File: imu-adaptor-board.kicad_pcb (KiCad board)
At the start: 2 copper layers, 49.5 x 49.5 mm, 7 parts, among them M3_MOUNT VAL**, P1 IMU-CAN, P2 IMU-SPI3, U1 ADIS16405BMLZ

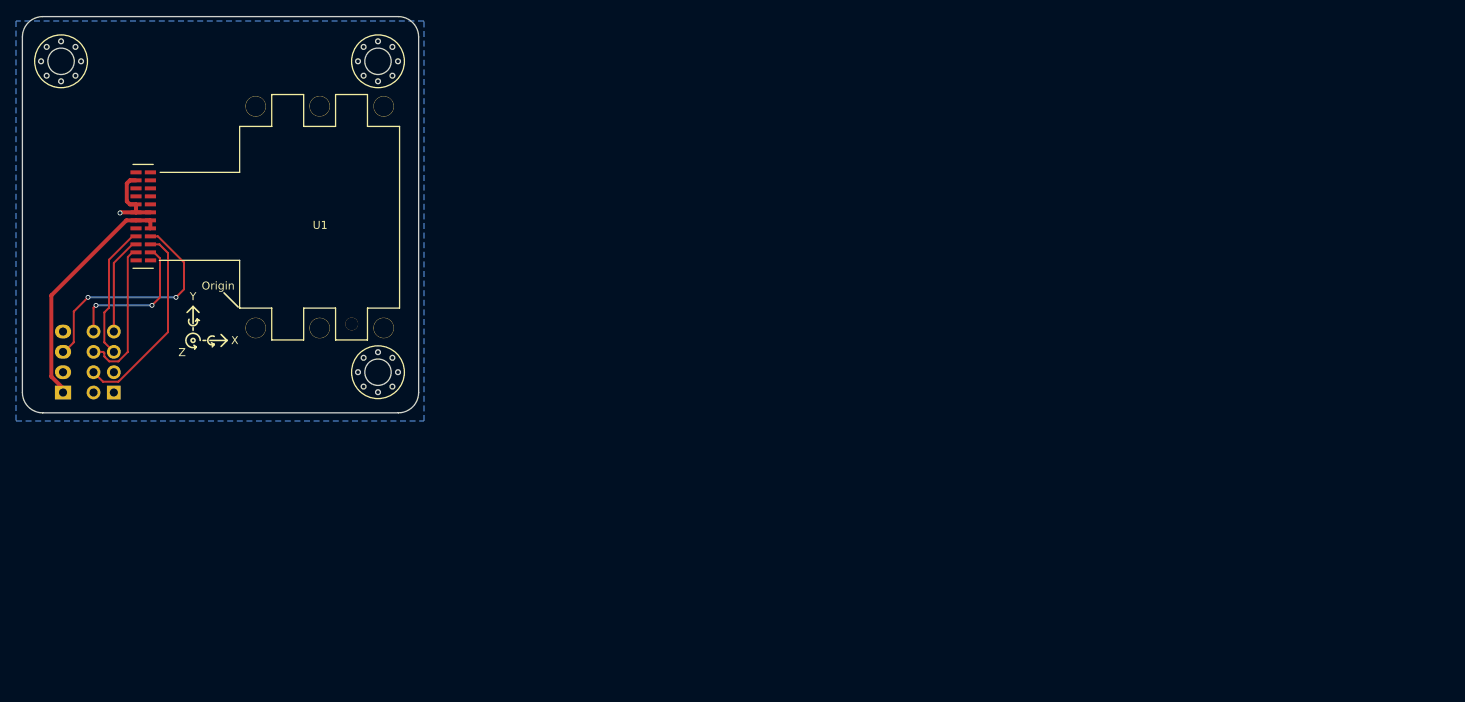
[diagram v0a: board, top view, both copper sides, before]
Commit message: place parts so they line up with imu board
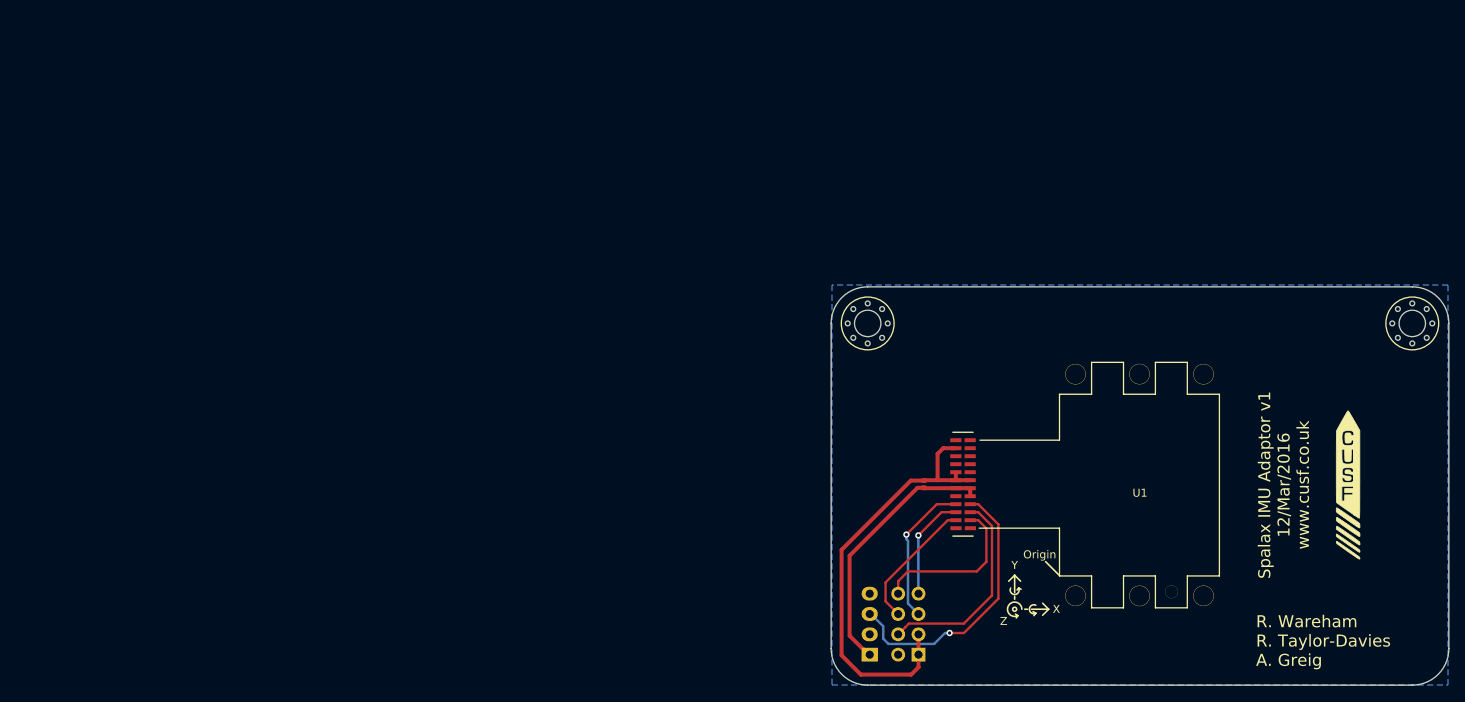
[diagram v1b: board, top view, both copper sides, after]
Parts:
- removed the M3_MOUNT at (95.2, 88.9)
- added C1: 100n, imu-adaptor-board:0402, F.Cu at (163.5, 102.9)
- G***: moved to F.Cu
- moved G*** 163.0 mm to (216.5, 103.0), turned to 0 degrees
- moved M3_MOUNT 133.4 mm to (224.5, 82.8)
- moved U1 107.8 mm to (190.5, 103.0)
- moved P1 106.0 mm to (156.7, 124.2)
- moved M3_MOUNT 106.0 mm to (156.5, 82.8)
- moved P2 105.8 mm to (162.8, 124.2)
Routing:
- net GND: track 9.68 -> 54.9 mm, vias 1 -> 0
- net /CAN1_TX: track 29.5 -> 34.7 mm, vias 2 -> 1
- net +5V: track 30.0 -> 33.1 mm
- net /SPI3_SCK: track 18.7 -> 16.6 mm
- net /SPI3_MISO: track 18.2 -> 20.2 mm, vias 2 -> 0
- net /DATA_RDY: track 16.8 -> 18.3 mm, vias 0 -> 1
- net /SPI3_NSS: track 24.9 -> 25.9 mm
- net /SPI3_MOSI: track 12.3 -> 13.2 mm, vias 0 -> 1
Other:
- board size 49.5 x 49.5 mm -> 77.2 x 49.8 mm
- board text added: "R. Wareham R. Taylor-Davies A. Greig"
- board text removed: "R. Wareham R. Taylor-Davies"

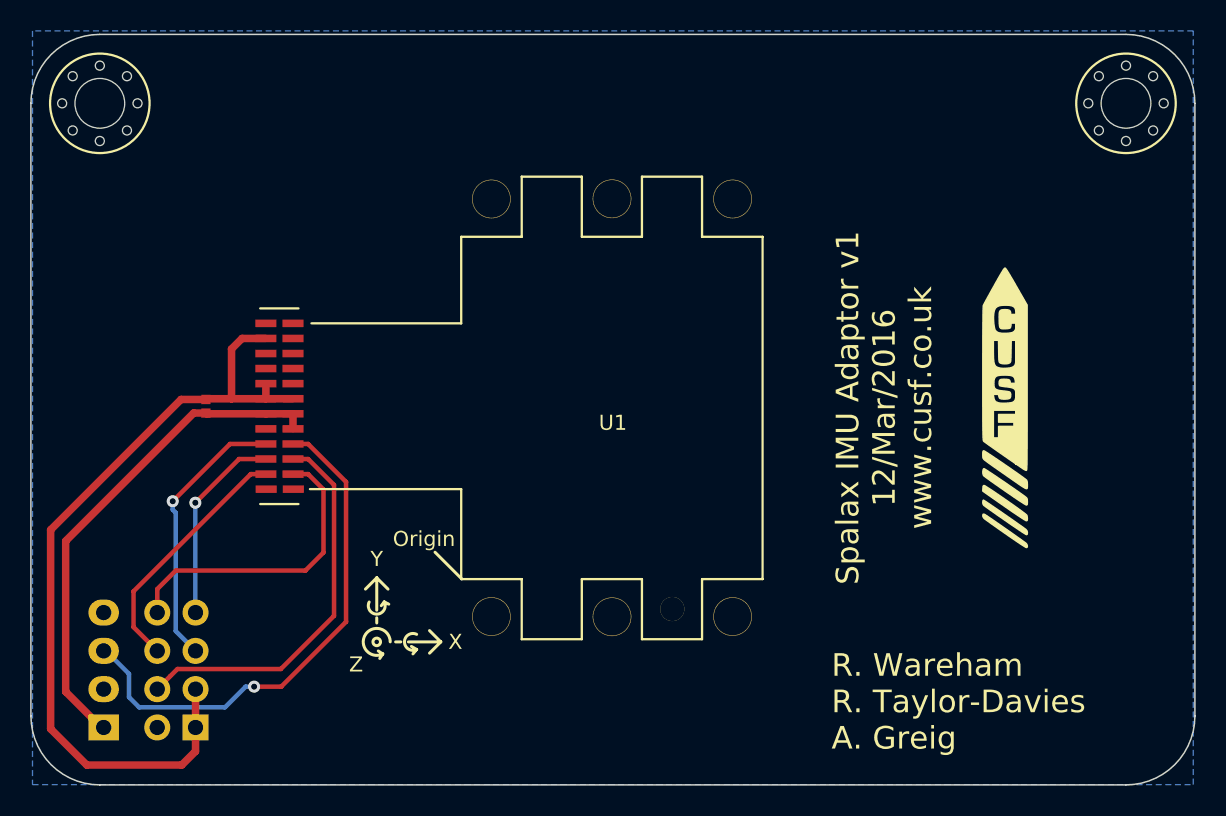
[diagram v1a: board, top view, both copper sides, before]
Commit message: change board outline to give access to ports/LEDs below
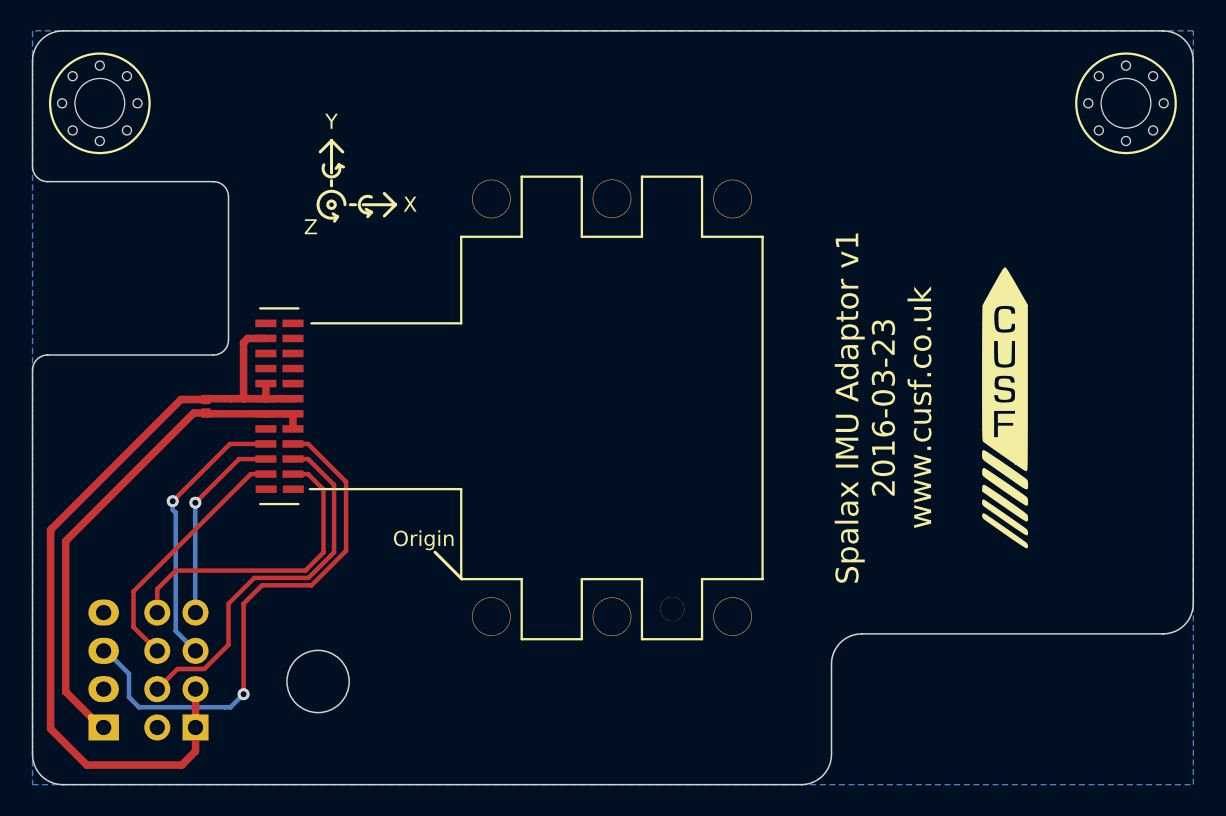
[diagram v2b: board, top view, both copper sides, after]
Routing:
- net /SPI3_NSS: track 25.9 -> 25.0 mm
- net /CAN1_TX: track 34.7 -> 35.5 mm
- net GND: track 54.9 -> 54.3 mm
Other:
- board size 77.2 x 49.8 mm -> 77 x 50 mm
- board text added: "Spalax IMU Adaptor v1 2016-03-23 www.cusf.co.uk"
- board text removed: "R. Wareham R. Taylor-Davies A. Greig"
- board text removed: "Spalax IMU Adaptor v1 12/Mar/2016 www.cusf.co.uk"

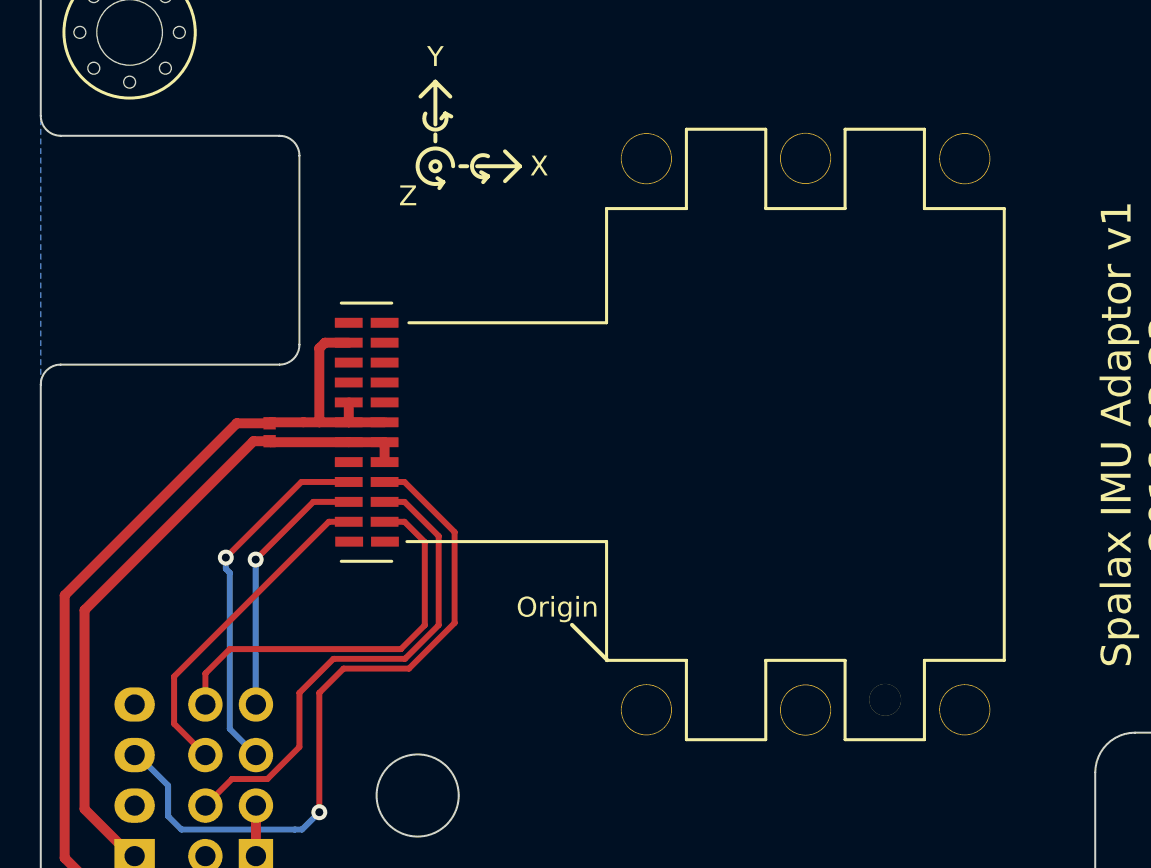
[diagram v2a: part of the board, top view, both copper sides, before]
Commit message: new ADIS16450BMLZ footprint, all 'done'
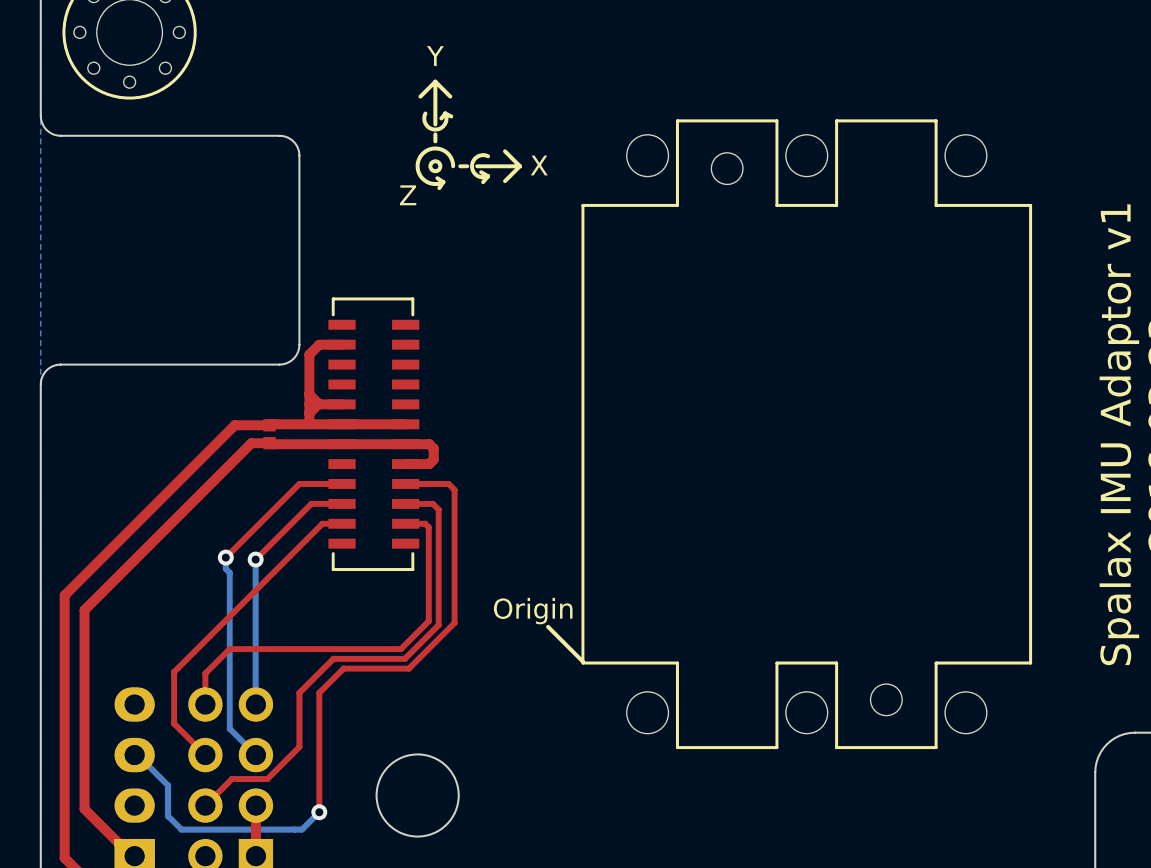
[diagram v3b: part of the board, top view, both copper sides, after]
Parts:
- moved C1 0.10 mm to (163.5, 103.0)
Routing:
- net +5V: track 33.1 -> 36.7 mm
- net GND: track 54.3 -> 56.9 mm

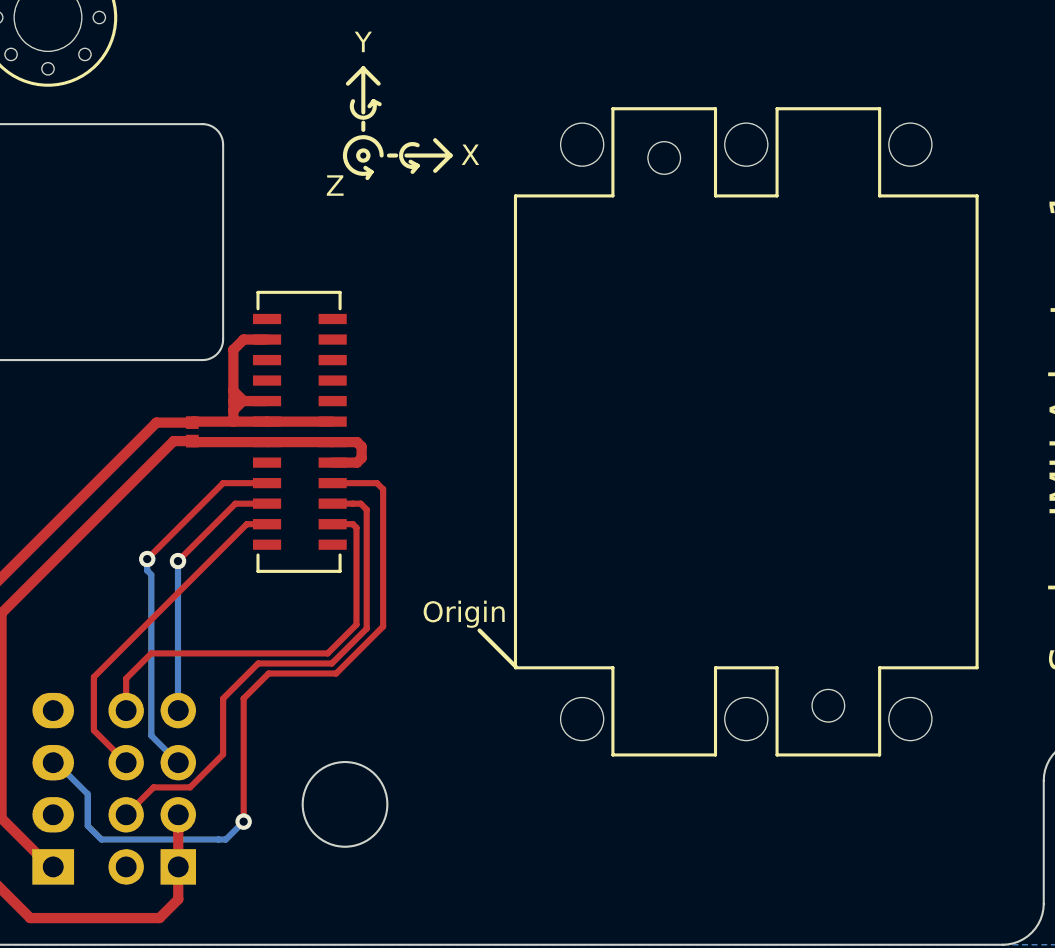
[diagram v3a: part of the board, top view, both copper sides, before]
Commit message: Use latest ADIS footprint
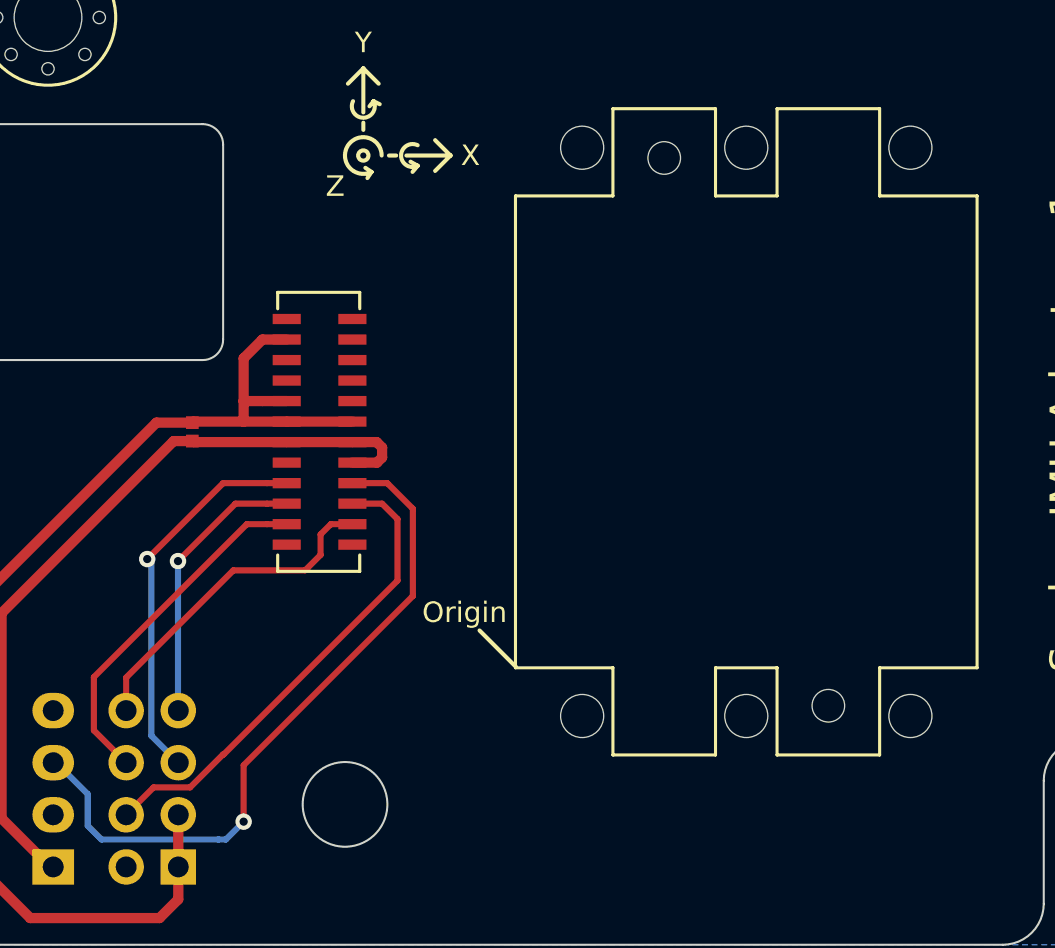
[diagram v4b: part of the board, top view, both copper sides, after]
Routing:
- net /SPI3_MISO: track 19.8 -> 16.3 mm
- net /CAN1_TX: track 35.6 -> 34.2 mm
- net /SPI3_NSS: track 24.7 -> 23.5 mm
- net +5V: track 36.7 -> 37.7 mm
- net /SPI3_SCK: track 16.4 -> 17.3 mm
- net /SPI3_MOSI: track 12.8 -> 13.8 mm
- net /DATA_RDY: track 17.9 -> 18.9 mm
- net GND: track 56.9 -> 57.6 mm
